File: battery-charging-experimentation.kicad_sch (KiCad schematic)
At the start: 24 parts, among them J1 USB_C_Receptacle_PowerOnly_6P, Q1 FS8205A, Q2 AO3415A, SW1 MK-12C08-G1.5, U2 DW01, U3 TP4056-42-ESOP8

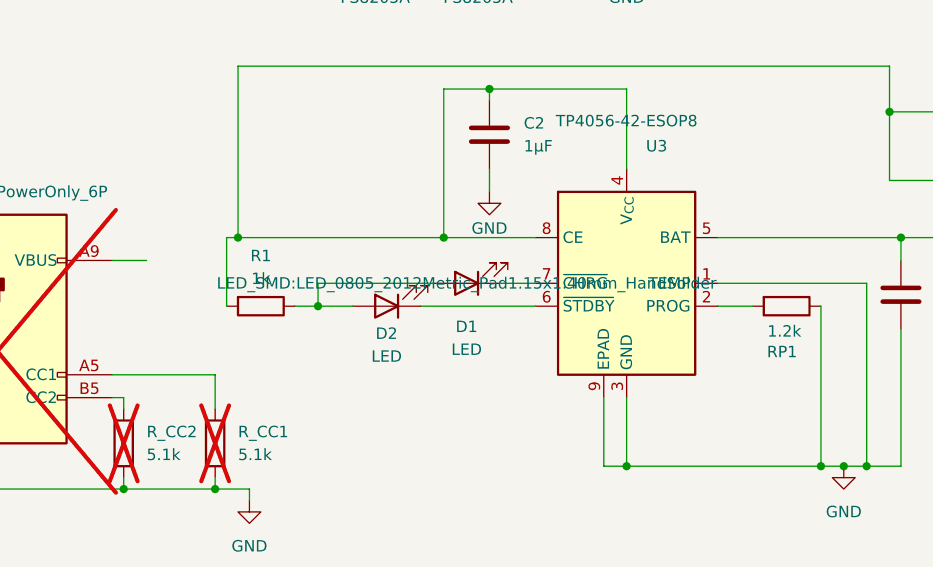
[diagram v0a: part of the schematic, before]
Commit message: update lcsc parts
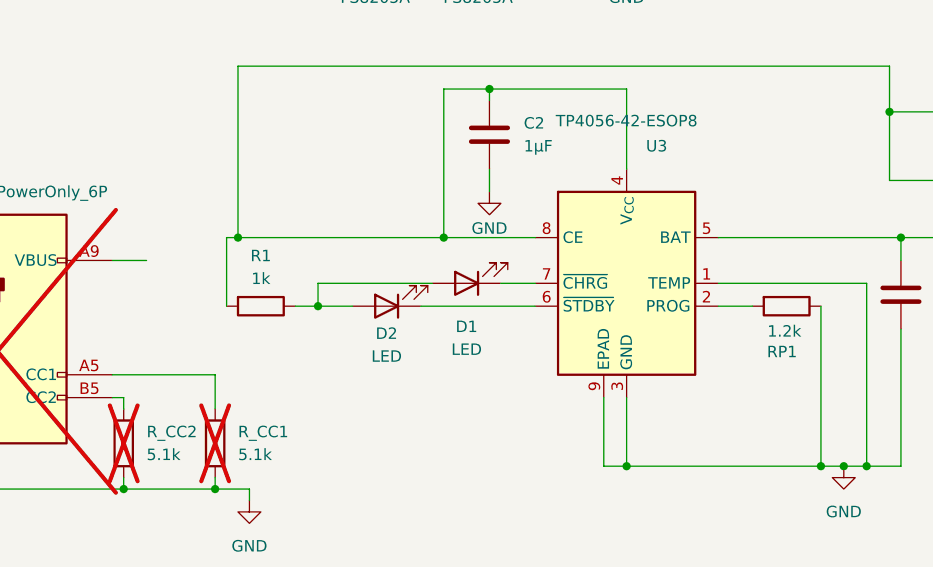
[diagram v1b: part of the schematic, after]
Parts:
- R2: LCSC Part C17414 -> C25744
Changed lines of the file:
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@@
 		)
 		(property "Footprint" "LED_SMD:LED_0805_2012Metric_Pad1.15x1.40mm_HandSolder"
-			(at 83.82 170.18 0)
-			(effects
-				(font
-					(size 1.27 1.27)
-				)
+			(at 85.09 181.864 0)
+			(effects
+				(font
+					(size 1.27 1.27)
+				)
+				(hide yes)
 			)
 		)
@@
 			)
 		)
-		(property "LCSC Part" "C17414"
+		(property "LCSC Part" "C25744"
 			(at 149.86 151.13 90)
 			(effects
